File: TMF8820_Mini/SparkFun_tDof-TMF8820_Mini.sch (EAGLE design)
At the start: 27 parts, among them J4 QWIIC_RIGHT_ANGLE, J5 QWIIC_RIGHT_ANGLE

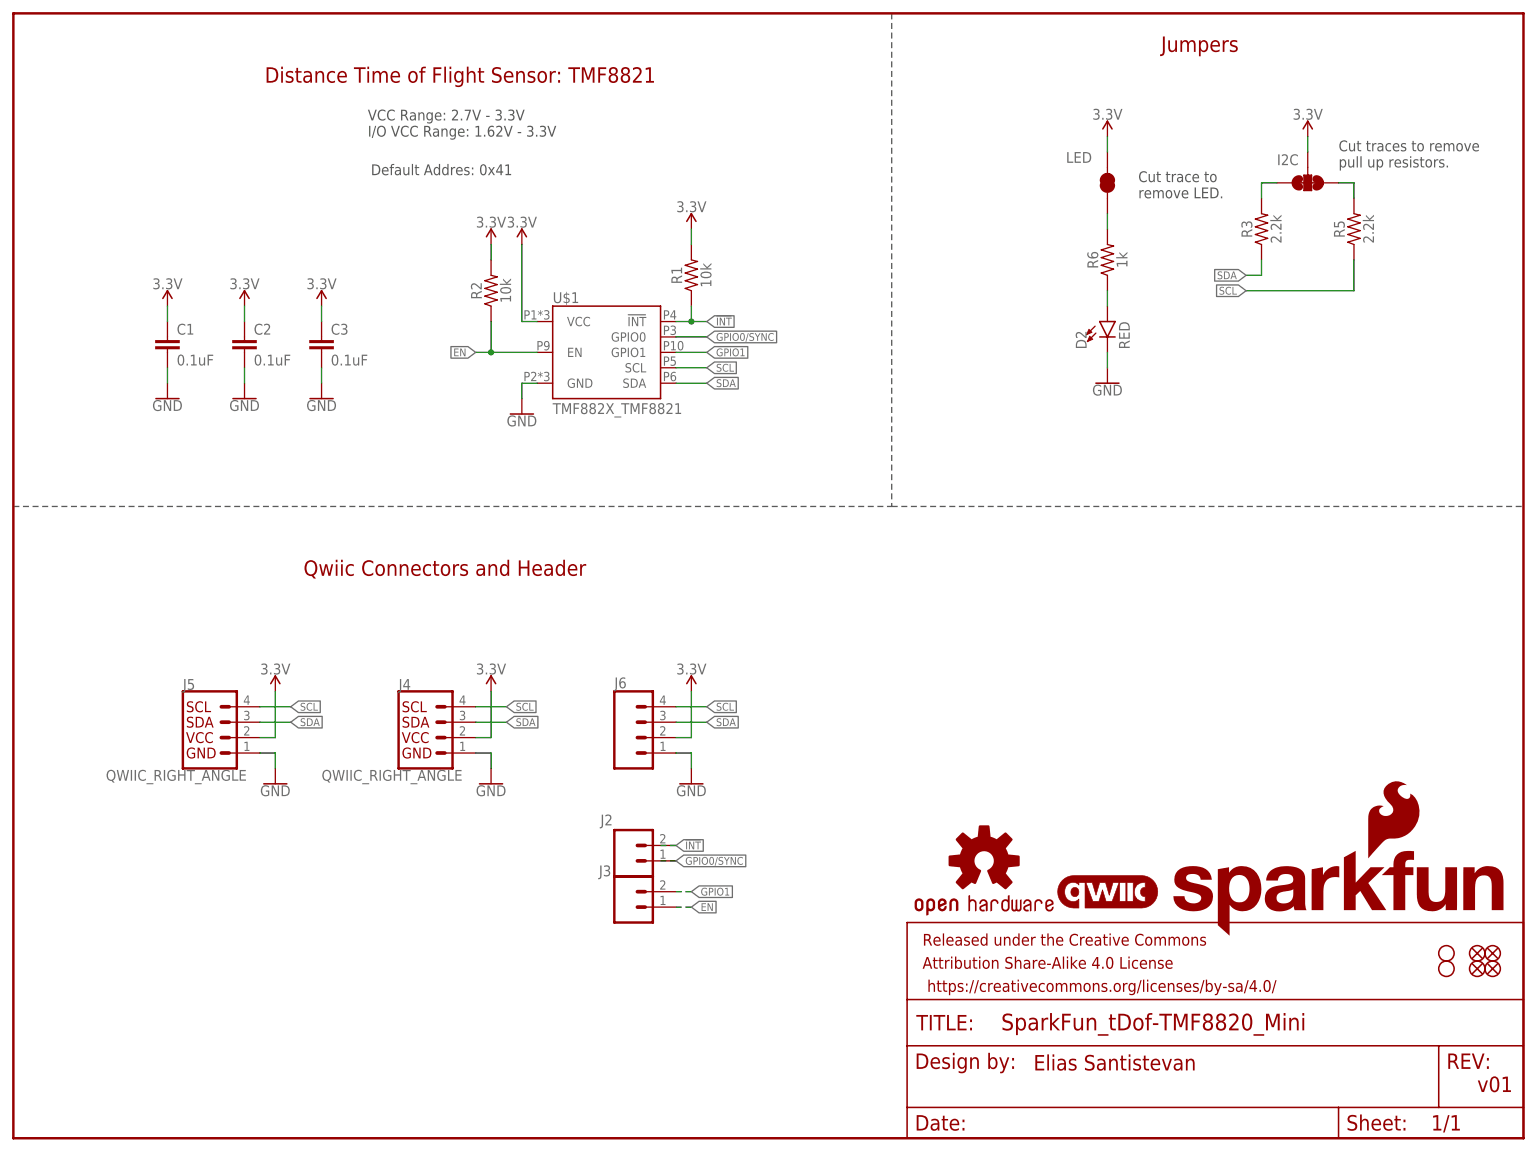
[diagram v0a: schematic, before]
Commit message: Removes old production files
* Removes old 8821 "HQ" variants
* Copies the 8820 and 8820 Mini variants
* Adjusts new 8820 copies to reference 8821 and replaces 8820 with 8821
* Updates Product Identifier jumpers to reflect changes
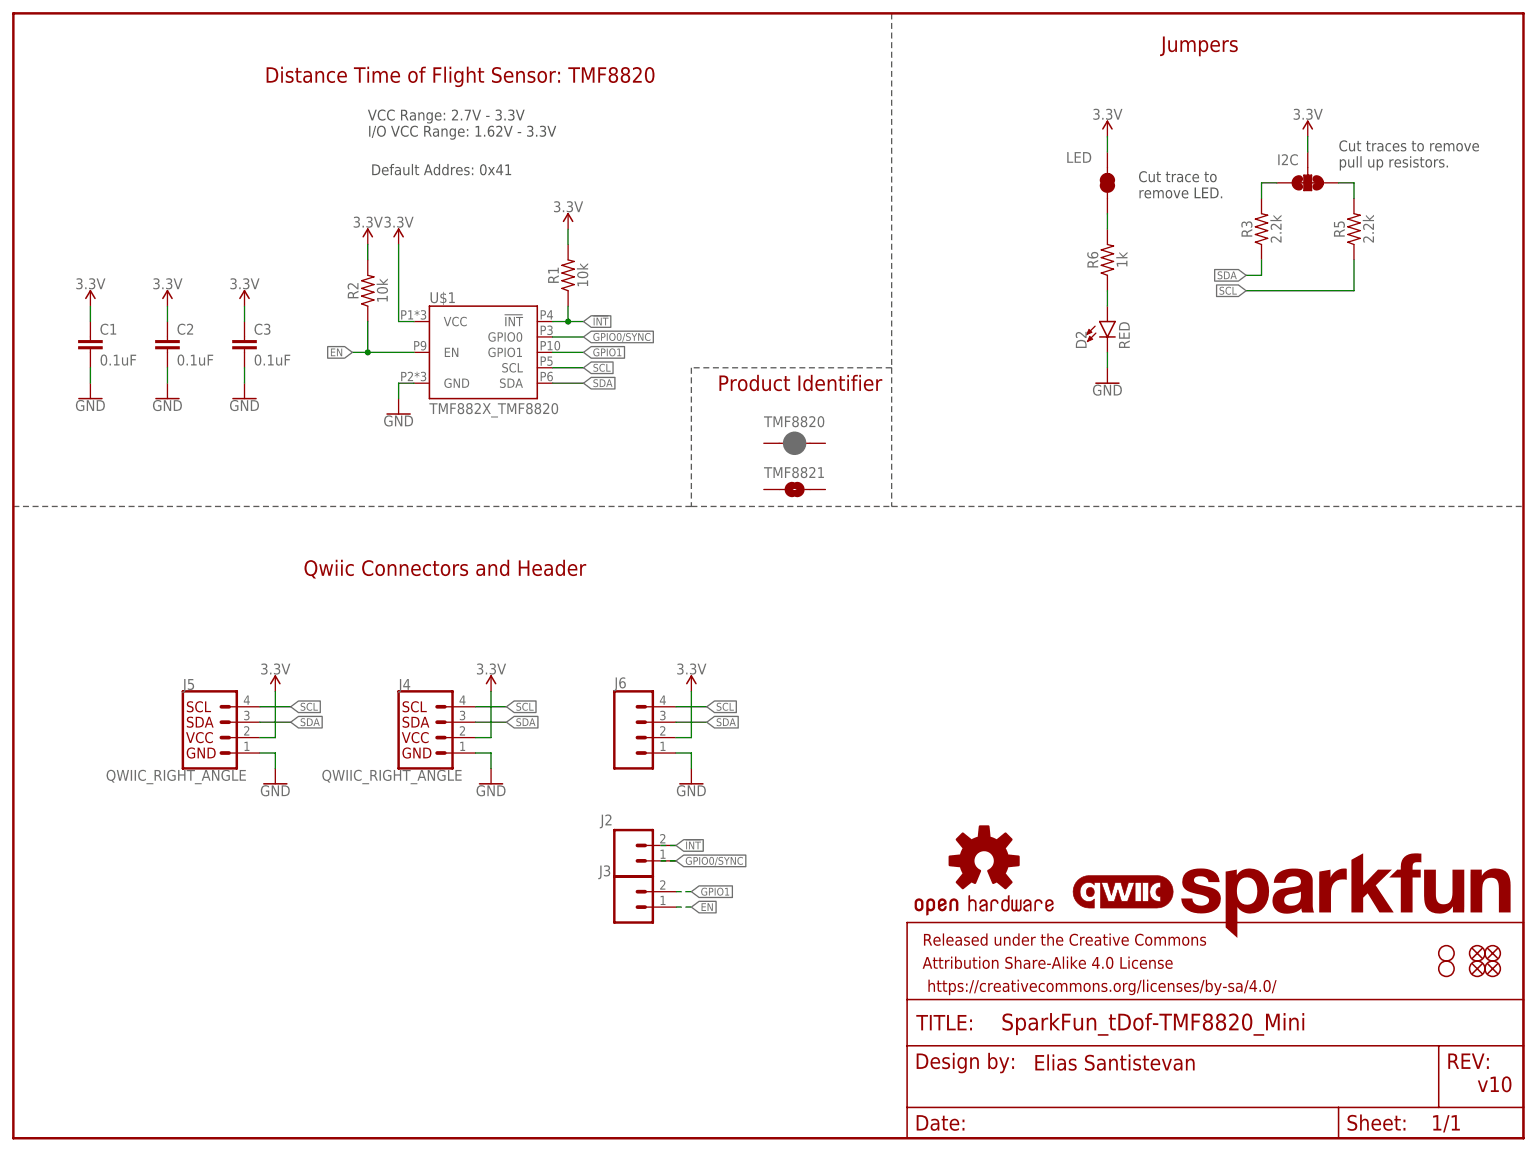
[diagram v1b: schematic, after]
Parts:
- added TMF8820: JUMPER-SMT_2_NC_PASTE_SILK, SparkFun-Jumpers:JUMPER-SMT_2_NC_PASTE_SILK
- added TMF8821: JUMPER-SMT_2_NO_SILK, SparkFun-Jumpers:JUMPER-SMT_2_NO_SILK
- LOGO1: value SFE_LOGO_NAME_FLAMEBLANK -> SFE_LOGO_NAMEBLANK; device SparkFun-Aesthetics:SFE_LOGO_NAME_FLAMEBLANK -> SparkFun-Aesthetics:SFE_LOGO_NAMEBLANK
- U$1: value TMF882X_TMF8821 -> TMF882X_TMF8820; device TMF882X:TMF882X_TMF8821 -> TMF882X:TMF882X_TMF8820
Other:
- note added: "Distance Time of Flight Sensor: TMF8820"
- note added: "Product Identifier"
- note added: "v10"
- note removed: "Distance Time of Flight Sensor: TMF8821"
- note removed: "v01"
- moved on the sheet: C1, C2, C3, R1, R2, U$1

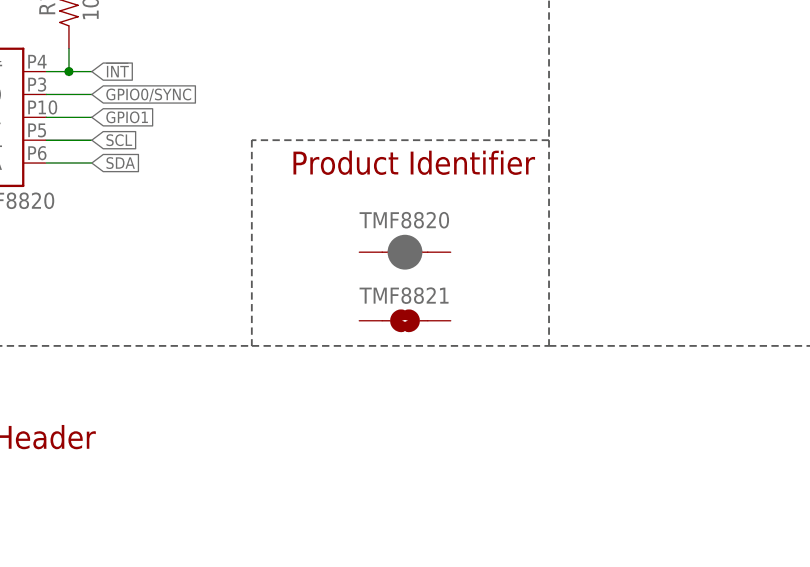
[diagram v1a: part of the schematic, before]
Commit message: Adds new product identifier pads to all designs, rolls 8820 version number to v10
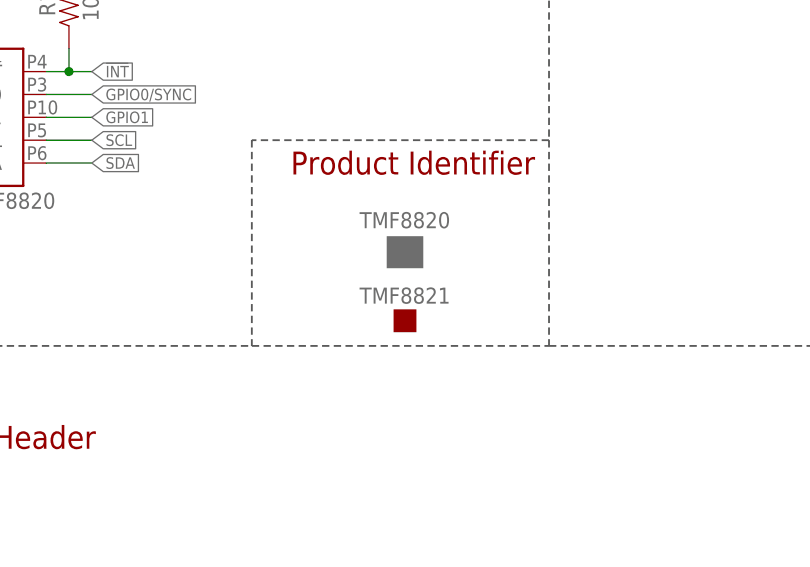
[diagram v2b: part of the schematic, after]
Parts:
- TMF8820: value JUMPER-SMT_2_NC_PASTE_SILK -> PROD_ID_PASTE_SILK; device SparkFun-Jumpers:JUMPER-SMT_2_NC_PASTE_SILK -> SparkFun-Aesthetics:PROD_ID_PASTE_SILK
- TMF8821: value JUMPER-SMT_2_NO_SILK -> PROD_ID_NO-PASTE_SILK; device SparkFun-Jumpers:JUMPER-SMT_2_NO_SILK -> SparkFun-Aesthetics:PROD_ID_NO-PASTE_SILK
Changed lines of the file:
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@@
 <part name="LOGO2" library="SparkFun-Aesthetics" deviceset="QWIIC_LOGO" device="_3MM"/>
 <part name="LOGO3" library="SparkFun-Aesthetics" deviceset="OSHW-LOGO" device="NO_SILK"/>
-<part name="TMF8820" library="SparkFun-Jumpers" deviceset="JUMPER-SMT_2_NC_PASTE" device="_SILK" package3d_urn="urn:adsk.eagle:package:39282/1"/>
-<part name="TMF8821" library="SparkFun-Jumpers" deviceset="JUMPER-SMT_2_NO" device="_SILK" package3d_urn="urn:adsk.eagle:package:39279/1"/>
+<part name="TMF8820" library="SparkFun-Aesthetics" deviceset="PROD_ID_PASTE" device="_SILK"/>
+<part name="TMF8821" library="SparkFun-Aesthetics" deviceset="PROD_ID_NO-PASTE" device="_SILK"/>
 </parts>
 <sheets>

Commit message: Changes all "IO" silk to be "GP" instead, increases Qwiic pill size on mini's
* Fixes orientation of I2C and LED silk on mini versions
* Increases SparkFun flame size on mini versions
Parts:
- LOGO2: value QWIIC_LOGO_3MM -> QWIIC_LOGO_4MM; device SparkFun-Aesthetics:QWIIC_LOGO_3MM -> SparkFun-Aesthetics:QWIIC_LOGO_4MM
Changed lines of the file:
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@@
 <part name="J3" library="SparkFun-Connectors" deviceset="CONN_02" device="1X02_NO_SILK"/>
 <part name="LOGO1" library="SparkFun-Aesthetics" deviceset="SFE_LOGO_NAME" device="BLANK"/>
-<part name="LOGO2" library="SparkFun-Aesthetics" deviceset="QWIIC_LOGO" device="_3MM"/>
+<part name="LOGO2" library="SparkFun-Aesthetics" deviceset="QWIIC_LOGO" device="_4MM" value="QWIIC_LOGO_4MM"/>
 <part name="LOGO3" library="SparkFun-Aesthetics" deviceset="OSHW-LOGO" device="NO_SILK"/>
 <part name="TMF8820" library="SparkFun-Aesthetics" deviceset="PROD_ID_PASTE" device="_SILK"/>
